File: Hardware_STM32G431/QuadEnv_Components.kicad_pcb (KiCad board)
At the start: 2 copper layers, 18.8 x 93 mm, 62 parts, among them J1 Conn_01x04_Male, J2 Conn_01x04_Male, J3 Conn_01x04_Male, J4 Conn_01x04_Male, J5 SWD_Header, J6 Eurorack_10_pin_power, J7 USB_B_Micro, U1 STM32G431C6T6, U2 LD1117-3.3-4Tab, U3 CD40109B, U4 TL074

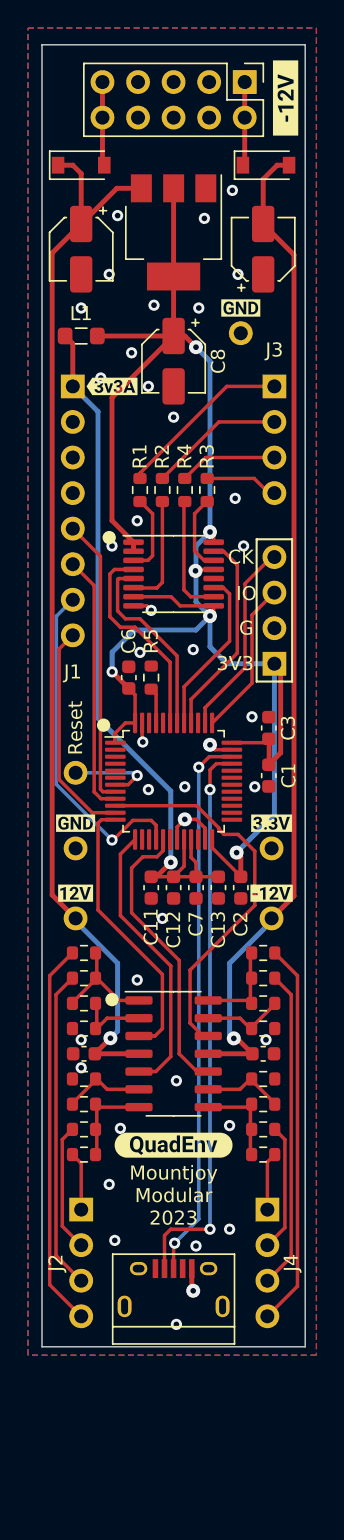
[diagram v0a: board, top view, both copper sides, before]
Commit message: First draft of control PCB complete
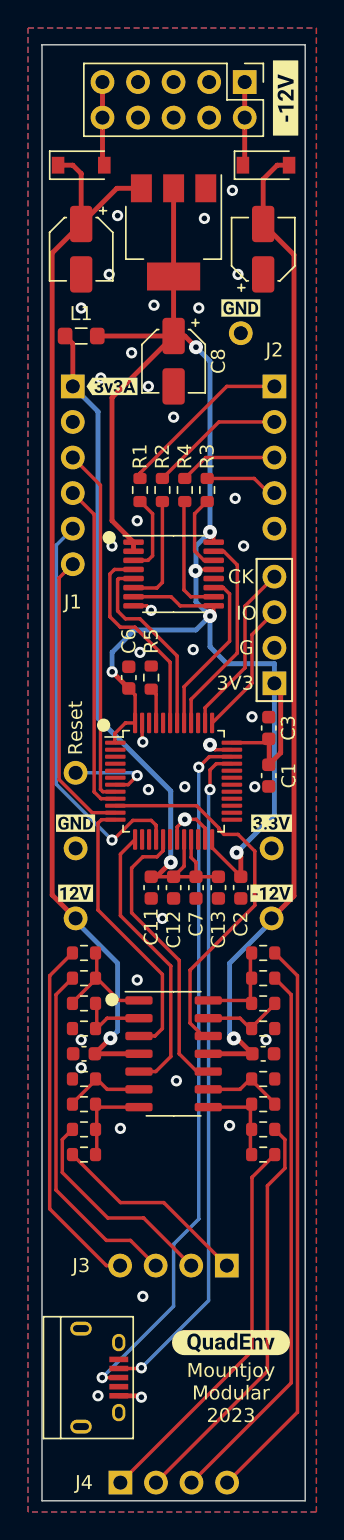
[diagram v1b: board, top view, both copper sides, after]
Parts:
- J1: footprint Connector_PinHeader_2.54mm:PinHeader_1x08_P2.54mm_Vertical -> Connector_PinHeader_2.54mm:PinHeader_1x06_P2.54mm_Vertical
- J2: renamed from J3; value Conn_01x04_Male -> Conn_01x05_Male; footprint Connector_PinHeader_2.54mm:PinHeader_1x04_P2.54mm_Vertical -> Connector_PinHeader_2.54mm:PinHeader_1x05_P2.54mm_Vertical
- moved J4 22.1 mm to (55.6, 152.7), turned to -90 degrees
- moved kibuzzard-640A0C12 14.7 mm to (63.5, 142.7)
- moved J3 11.1 mm to (63.2, 137.2), turned to 90 degrees
- moved J7 8.31 mm to (54.1, 145.2), turned to -90 degrees
- moved J5 1.40 mm to (66.6, 95.6)
- renumbered J2 to J3
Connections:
- J1 pad 3: GND -> /Attack_Pot
- J1 pad 4: GND -> /Decay_Pot
- J1 pad 5: /Attack_Pot -> /Release_Pot
- J1 pad 6: /Decay_Pot -> /Sustain_Pot
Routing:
- net /Led3_Out: track 4.15 -> 28.0 mm
- net /Env3_Out: track 9.09 -> 29.3 mm
- net /Led4_Out: track 22.8 -> 39.5 mm
- net /Env4_Out: track 27.5 -> 40.6 mm
- net /USB_DP: track 39.2 -> 50.3 mm
- net /Led2_Out: track 4.19 -> 14.3 mm
- net /USB_DM: track 40.4 -> 48.2 mm
- net /Env2_Out: track 9.13 -> 15.3 mm
- net /Sustain_Pot: track 15.7 -> 20.8 mm
- net /Release_Pot: track 24.2 -> 29.3 mm
- net /Decay_Pot: track 18.6 -> 23.7 mm
- net /Attack_Pot: track 20.6 -> 25.6 mm
- net /Led1_Out: track 22.8 -> 25.0 mm
- net /Env1_Out: track 27.6 -> 25.7 mm
- net +3.3V: track 120.7 -> 119.3 mm
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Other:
- board size 18.8 x 93 mm -> 18.8 x 104 mm

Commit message: First draft of Panel complete
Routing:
- net GND: vias 37 -> 43
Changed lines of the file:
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@@
   (gr_circle (center 54.8 85.2) (end 55.2 85.2) (layer "F.SilkS") (width 0.15) (fill solid))
   (gr_circle (center 55 118.2) (end 55.4 118.2) (layer "F.SilkS") (width 0.15) (fill solid))
-  (gr_circle (center 54.4 98.6) (end 54.8 98.6) (layer "F.SilkS") (width 0.15) (fill solid))
+  (gr_circle (center 53.9 99.4) (end 54.3 99.4) (layer "F.SilkS") (width 0.15) (fill solid))
   (gr_line locked (start 59.4 48.3) (end 59.4 161.5) (layer "Dwgs.User") (width 0.15))
   (gr_rect (start 50 50) (end 68.8 154) (layer "Edge.Cuts") (width 0.1) (fill none))
@@
   (via (at 54.8 66.4) (size 0.8) (drill 0.4) (layers "F.Cu" "B.Cu") (free) (net 2))
   (via (at 56.4 72) (size 0.8) (drill 0.4) (layers "F.Cu" "B.Cu") (free) (net 2))
-  (via (at 54.2 73.8) (size 0.8) (drill 0.4) (layers "F.Cu" "B.Cu") (free) (net 2))
+  (via (at 54.1 73.3) (size 0.8) (drill 0.4) (layers "F.Cu" "B.Cu") (free) (net 2))
   (via (at 57.1 146.6) (size 0.8) (drill 0.4) (layers "F.Cu" "B.Cu") (free) (net 2))
   (via (at 63.4 127.2) (size 0.8) (drill 0.4) (layers "F.Cu" "B.Cu") (free) (net 2))
   (via (at 55 85.8) (size 0.8) (drill 0.4) (layers "F.Cu" "B.Cu") (free) (net 2))
+  (via (at 63.5 139.6) (size 0.8) (drill 0.4) (layers "F.Cu" "B.Cu") (free) (net 2))
   (via (at 62 100) (size 1) (drill 0.4) (layers "F.Cu" "B.Cu") (net 2))
+  (via (at 63.5 135) (size 0.8) (drill 0.4) (layers "F.Cu" "B.Cu") (free) (net 2))
   (via (at 57.2 99.8) (size 0.8) (drill 0.4) (layers "F.Cu" "B.Cu") (free) (net 2))
   (via (at 63.8 82.4) (size 0.8) (drill 0.4) (layers "F.Cu" "B.Cu") (free) (net 2))
+  (via (at 51.9 152) (size 0.8) (drill 0.4) (layers "F.Cu" "B.Cu") (free) (net 2))
   (via (at 60.8 93.2) (size 0.8) (drill 0.4) (layers "F.Cu" "B.Cu") (free) (net 2))
   (via (at 59.6 124) (size 0.8) (drill 0.4) (layers "F.Cu" "B.Cu") (free) (net 2))
@@
   (via (at 52.8 68.8) (size 0.8) (drill 0.4) (layers "F.Cu" "B.Cu") (free) (net 2))
   (via (at 52.8 123.07) (size 0.8) (drill 0.4) (layers "F.Cu" "B.Cu") (free) (net 2))
+  (via (at 59.7 131.5) (size 0.8) (drill 0.4) (layers "F.Cu" "B.Cu") (free) (net 2))
   (via (at 55.6 127.4) (size 0.8) (drill 0.4) (layers "F.Cu" "B.Cu") (free) (net 2))
+  (via (at 51.3 136.1) (size 0.8) (drill 0.4) (layers "F.Cu" "B.Cu") (free) (net 2))
   (via (at 64 66.4) (size 0.8) (drill 0.4) (layers "F.Cu" "B.Cu") (free) (net 2))
   (via (at 57.8 90.4) (size 0.8) (drill 0.4) (layers "F.Cu" "B.Cu") (free) (net 2))
   (via (at 57 93.4) (size 0.8) (drill 0.4) (layers "F.Cu" "B.Cu") (free) (net 2))
+  (via (at 66.9 152.4) (size 0.8) (drill 0.4) (layers "F.Cu" "B.Cu") (free) (net 2))
   (via (at 55.4 62.2) (size 0.8) (drill 0.4) (layers "F.Cu" "B.Cu") (free) (net 2))
   (via (at 65 98) (size 0.8) (drill 0.4) (layers "F.Cu" "B.Cu") (free) (net 2))
@@
   (segment (start 56.4 108.8) (end 56.4 112) (width 0.25) (layer "F.Cu") (net 40))
   (segment (start 59.8 122.07) (end 61.07 123.34) (width 0.25) (layer "F.Cu") (net 40))
+  (segment (start 56.490685 105.4) (end 55.295343 106.595343) (width 0.25) (layer "F.Cu") (net 42))
+  (segment (start 58.15 106.7625) (end 58.15 105.75) (width 0.25) (layer "F.Cu") (net 42))
   (segment (start 57.8 105.4) (end 56.490685 105.4) (width 0.25) (layer "F.Cu") (net 42))
-  (segment (start 55.090685 106.8) (end 55 106.8) (width 0.25) (layer "F.Cu") (net 42))
-  (segment (start 56.490685 105.4) (end 55.090685 106.8) (width 0.25) (layer "F.Cu") (net 42))
   (segment (start 58.15 105.75) (end 57.8 105.4) (width 0.25) (layer "F.Cu") (net 42))
-  (segment (start 58.15 106.7625) (end 58.15 105.75) (width 0.25) (layer "F.Cu") (net 42))
-  (via (at 55 106.8) (size 0.8) (drill 0.4) (layers "F.Cu" "B.Cu") (net 42))
-  (segment (start 55 106.8) (end 51.025 102.825) (width 0.25) (layer "B.Cu") (net 42))
-  (segment (start 51.025 102.825) (end 51.025 90.815) (width 0.25) (layer "B.Cu") (net 42))
-  (segment (start 51.025 90.815) (end 51.025 85.735) (width 0.25) (layer "B.Cu") (net 42))
-  (segment (start 51.025 85.735) (end 52.2 84.56) (width 0.25) (layer "B.Cu") (net 42))
+  (via (at 55.295343 106.595343) (size 0.8) (drill 0.4) (layers "F.Cu" "B.Cu") (net 42))
+  (segment (start 51.025 85.735) (end 51.025 102.325) (width 0.25) (layer "B.Cu") (net 42))
+  (segment (start 52.2 84.56) (end 51.025 85.735) (width 0.25) (layer "B.Cu") (net 42))
+  (segment (start 51.025 102.325) (end 55.295343 106.595343) (width 0.25) (layer "B.Cu") (net 42))
   (segment (start 66.6 87.99) (end 64.5 90.09) (width 0.25) (layer "F.Cu") (net 53))
   (segment (start 61.65 97.35) (end 61.65 98.4375) (width 0.25) (layer "F.Cu") (net 53))

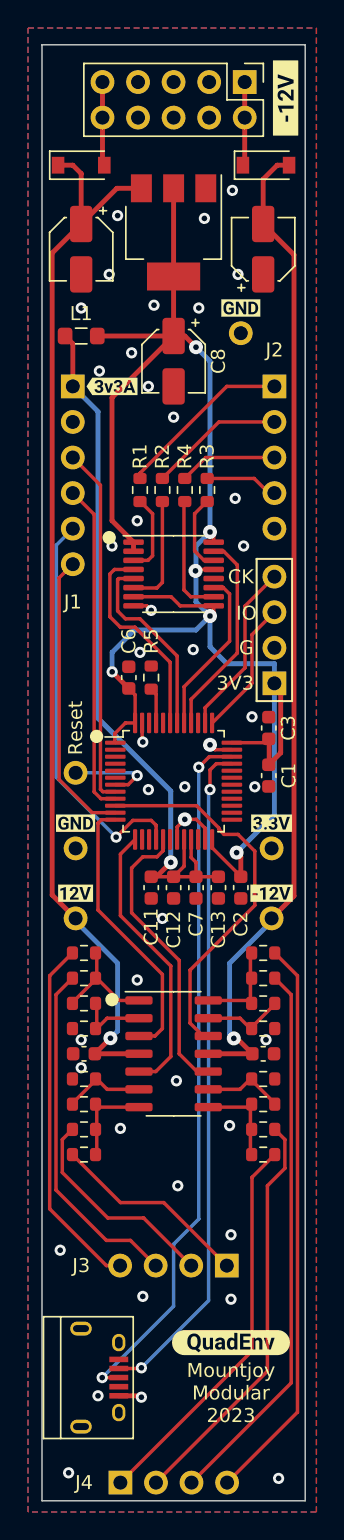
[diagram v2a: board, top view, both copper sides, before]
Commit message: Clean up project for manufacture
Fixed LED ordering bug on control board
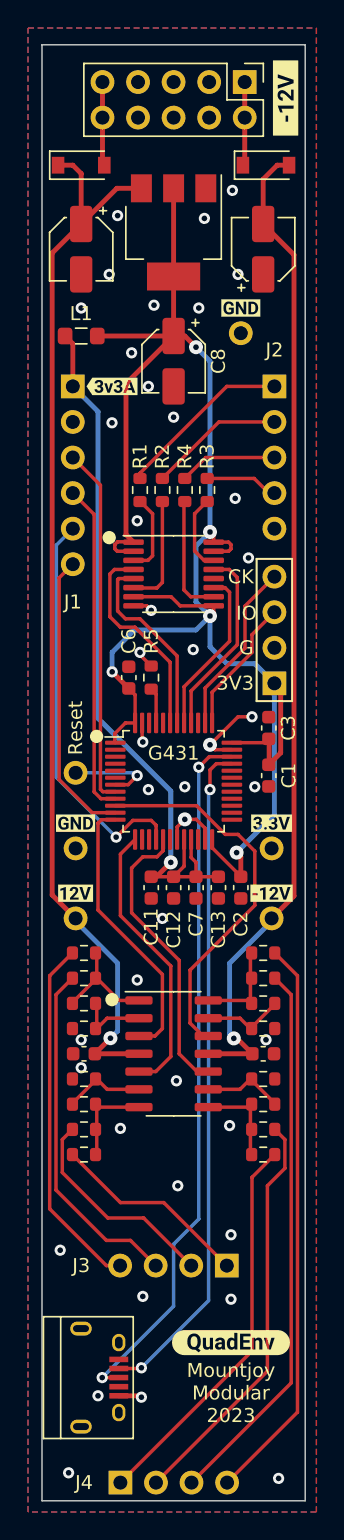
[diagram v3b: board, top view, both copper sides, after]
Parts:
- J1: footprint Connector_PinHeader_2.54mm:PinHeader_1x06_P2.54mm_Vertical -> Connector_PinSocket_2.54mm:PinSocket_1x06_P2.54mm_Vertical
- J2: footprint Connector_PinHeader_2.54mm:PinHeader_1x05_P2.54mm_Vertical -> Connector_PinSocket_2.54mm:PinSocket_1x05_P2.54mm_Vertical
- J3, J4: footprint Connector_PinHeader_2.54mm:PinHeader_1x04_P2.54mm_Vertical -> Connector_PinSocket_2.54mm:PinSocket_1x04_P2.54mm_Vertical
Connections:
- U3 pad 13: +3.3V -> /Gate4
- U3 pad 15: /Gate4 -> +3.3V
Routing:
- net GND: track 10.3 -> 15.5 mm, vias 43 -> 42
- net +3.3V: track 119.3 -> 121.8 mm, vias 6 -> 5
- net /Gate4: track 14.7 -> 13.7 mm
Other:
- board text added: "G431"

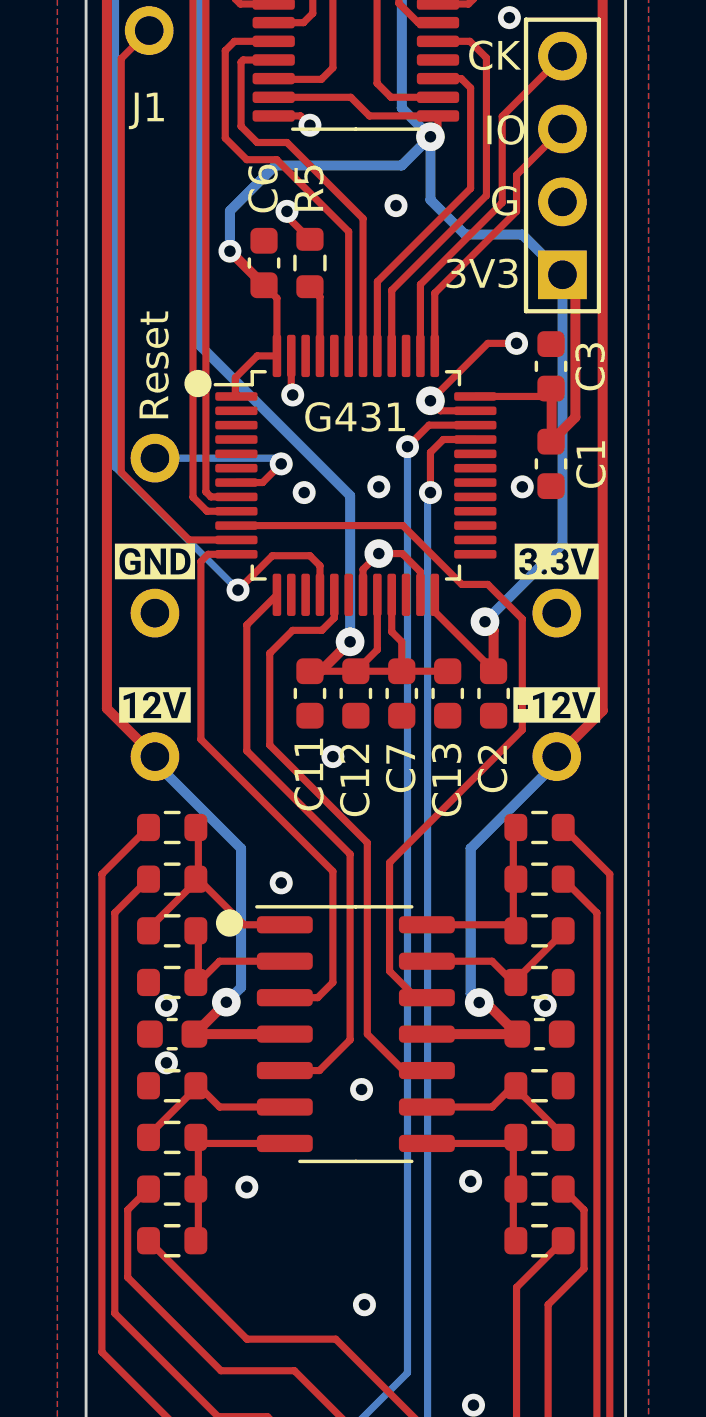
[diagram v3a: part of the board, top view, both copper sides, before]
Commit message: Corrections to schematic to fix sustain and release pots being switched
+Updated project to use production module parts and connections
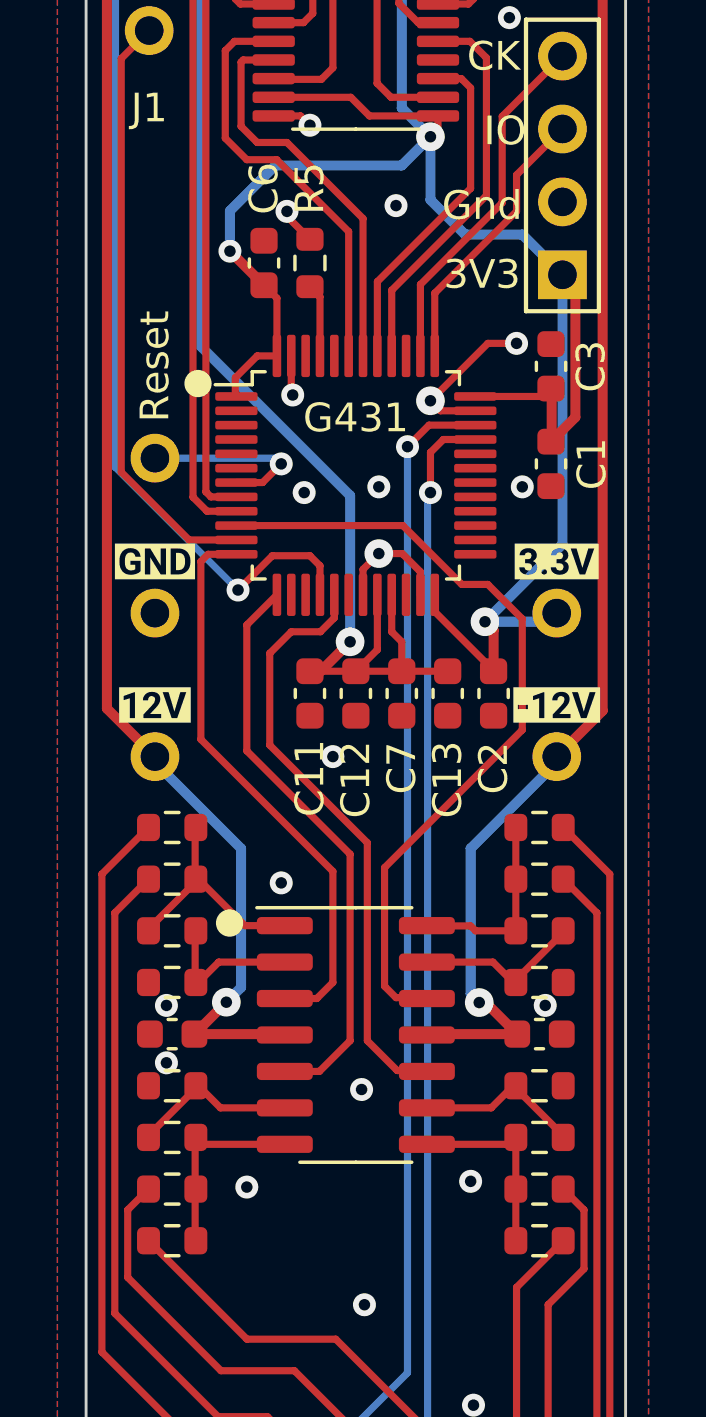
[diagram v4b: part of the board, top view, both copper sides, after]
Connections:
- J1 pad 5: /Release_Pot -> /Sustain_Pot
- J1 pad 6: /Sustain_Pot -> /Release_Pot
- TP2 pad 1: +3V3 -> +3.3V
- U1 pad 11: /Sustain_Pot -> /Release_Pot
- U1 pad 16: /Release_Pot -> /Sustain_Pot
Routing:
- net /Sustain_Pot: track 20.8 -> 28.8 mm, vias 0 -> 1
- net /Release_Pot: track 28.8 -> 20.8 mm, vias 1 -> 0
- net +3.3V: track 121.8 -> 124.4 mm
- net /Env4_DAC: track 27.2 -> 27.7 mm
